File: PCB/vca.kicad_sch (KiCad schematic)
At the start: 5 parts, among them J8 VCA, Q7 2N5457

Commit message: Necessary Changes to Schematic and PCB
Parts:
- J8: footprint Connector_PinHeader_2.00mm:PinHeader_1x02_P2.00mm_Vertical -> Connector_PinSocket_2.54mm:PinSocket_1x02_P2.54mm_Vertical
- Q7: footprint Package_TO_SOT_THT:TO-92_Inline -> Package_TO_SOT_THT:TO-92_Inline_Wide; symbol Simulation_SPICE:NJFET -> Device:Q_NJFET_DSG
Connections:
- net X13: now also Q7.2 (S); no longer Q7.3 (S)
- net at R41.2, R46.1: now also Q7.3 (G); no longer Q7.2 (G)
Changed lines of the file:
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@@
 	)
 	(symbol
-		(lib_id "Simulation_SPICE:NJFET")
+		(lib_id "Device:Q_NJFET_DSG")
 		(at 113.03 90.17 90)
 		(unit 1)
@@
 			)
 		)
-		(property "Footprint" "Package_TO_SOT_THT:TO-92_Inline"
+		(property "Footprint" "Package_TO_SOT_THT:TO-92_Inline_Wide"
 			(at 110.49 85.09 0)
 			(hide yes)
@@
 			)
 		)
-		(property "Description" ""
+		(property "Description" "N-JFET transistor, drain/source/gate"
 			(at 113.03 90.17 0)
 			(hide yes)
@@
 			)
 		)
-		(property "Sim.Pins" "1=D 2=G 3=S"
+		(property "Sim.Pins" "1=D 2=S 3=G"
 			(at 113.03 90.17 0)
 			(hide yes)
@@
 		)
 		(property "Value" "VCA"
-			(at 170.18 31.75 0)
+			(at 164.338 27.178 0)
 			(show_name no)
 			(do_not_autoplace no)
@@
 			)
 		)
-		(property "Footprint" "Connector_PinHeader_2.00mm:PinHeader_1x02_P2.00mm_Vertical"
+		(property "Footprint" "Connector_PinSocket_2.54mm:PinSocket_1x02_P2.54mm_Vertical"
 			(at 163.83 31.75 0)
 			(hide yes)

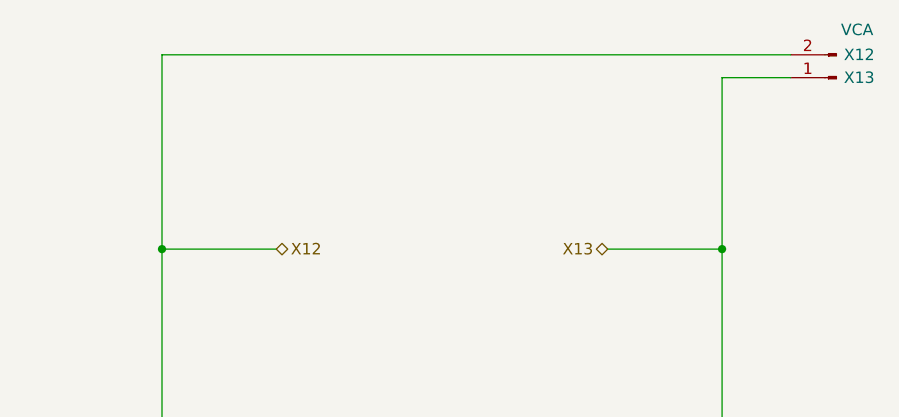
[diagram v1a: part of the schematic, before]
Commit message: Final Update
Move power pins closer to filter caps
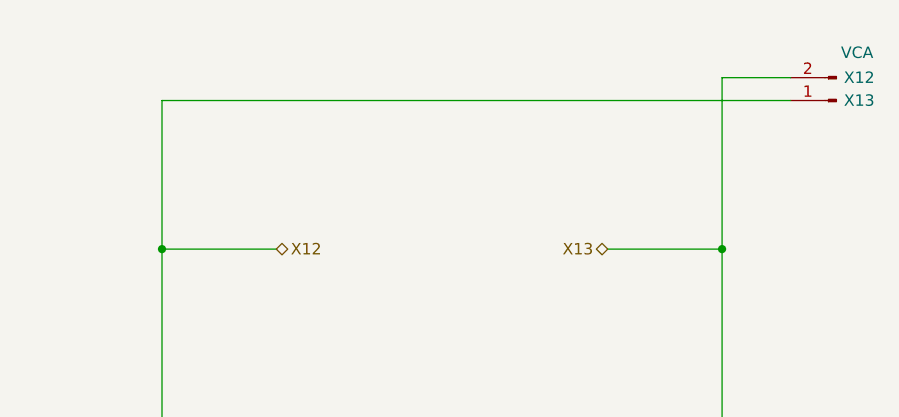
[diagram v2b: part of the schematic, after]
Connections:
- net FO: now also J8.1 (Pin_1); no longer J8.2 (Pin_2)
- net X13: now also J8.2 (Pin_2); no longer J8.1 (Pin_1)
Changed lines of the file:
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@@
 	(wire
 		(pts
-			(xy 88.9 29.21) (xy 88.9 50.8)
+			(xy 88.9 34.29) (xy 88.9 50.8)
 		)
 		(stroke
@@
 	(wire
 		(pts
-			(xy 158.75 29.21) (xy 88.9 29.21)
+			(xy 158.75 34.29) (xy 88.9 34.29)
 		)
 		(stroke
@@
 	(symbol
 		(lib_id "Connector:Conn_01x02_Pin")
-		(at 163.83 31.75 180)
+		(at 163.83 34.29 180)
 		(unit 1)
 		(body_style 1)
@@
 		(dnp no)
 		(property "Reference" "J8"
-			(at 165.1 29.21 0)
+			(at 165.1 31.75 0)
 			(hide yes)
 			(show_name no)
@@
 		)
 		(property "Value" "VCA"
-			(at 164.338 27.178 0)
+			(at 164.338 29.718 0)
 			(show_name no)
 			(do_not_autoplace no)
@@
 		)
 		(property "Footprint" "Connector_PinSocket_2.54mm:PinSocket_1x02_P2.54mm_Vertical"
-			(at 163.83 31.75 0)
+			(at 163.83 34.29 0)
 			(hide yes)
 			(show_name no)
@@
 		)
 		(property "Datasheet" ""
-			(at 163.83 31.75 0)
+			(at 163.83 34.29 0)
 			(hide yes)
 			(show_name no)
@@
 		)
 		(property "Description" ""
-			(at 163.83 31.75 0)
+			(at 163.83 34.29 0)
 			(hide yes)
 			(show_name no)
@@
 		)
 		(property "X13" "X13"
+			(at 166.37 34.29 0)
+			(show_name no)
+			(do_not_autoplace no)
+			(effects
+				(font
+					(size 1.27 1.27)
+				)
+			)
+		)
+		(property "X12" "X12"
 			(at 166.37 31.75 0)
 			(show_name no)
 			(do_not_autoplace no)
-			(effects
-				(font
-					(size 1.27 1.27)
-				)
-			)
-		)
-		(property "X12" "X12"
-			(at 166.37 29.21 0)
-			(show_name no)
-			(do_not_autoplace no)
